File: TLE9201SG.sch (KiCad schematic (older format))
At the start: 6 parts, among them U4 TLE9201SG

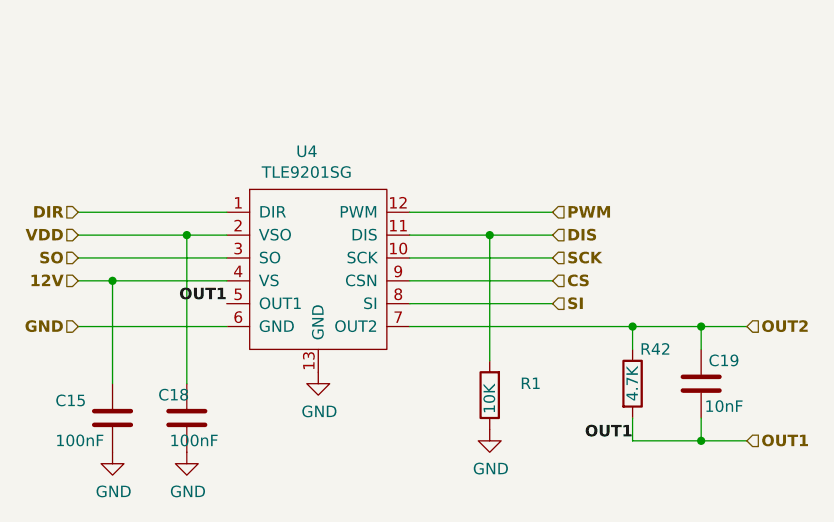
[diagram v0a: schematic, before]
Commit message: from Ola and Jared (#71)
* Update

* removed fp-info-cache from git

* Gerbers

* moved connector

* Mostly Ola's e-mailed copy, plus some of my own fixes to his almost done revision. I also did some house cleaning, with boundary edges, removed most DRC and ERC errors, etc.

* added Fiducial's
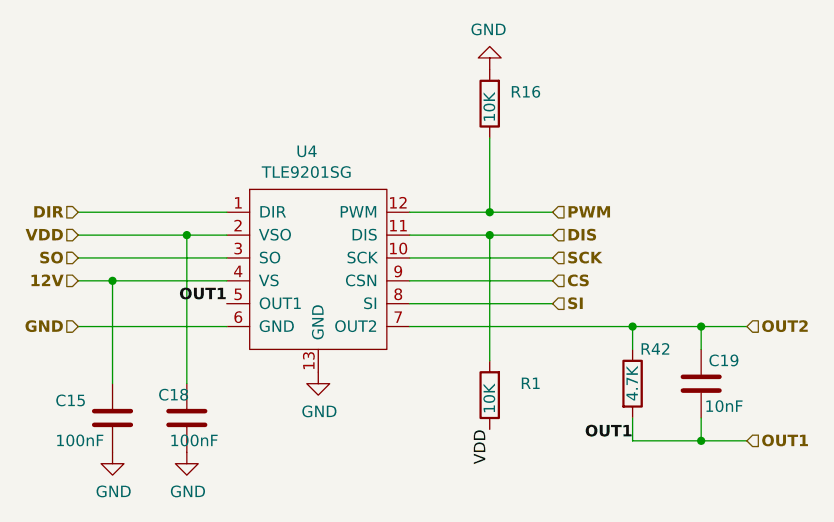
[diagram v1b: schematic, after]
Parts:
- added R16: 10K, Resistor_SMD:R_0603_1608Metric, symbol Device:R
- C15, C18, C19: footprint Capacitor_SMD:C_0603_1608Metric_Pad1.05x0.95mm_HandSolder -> Capacitor_SMD:C_0603_1608Metric
- R1, R42: footprint Resistor_SMD:R_0603_1608Metric_Pad1.05x0.95mm_HandSolder -> Resistor_SMD:R_0603_1608Metric
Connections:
- net GND: now also R16.2; no longer R1.1
- net PWM: now also R16.1
- net VDD: now also R1.1
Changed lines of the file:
@@
 EELAYER 29 0
 EELAYER END
-$Descr A4 11693 8268
+$Descr A 11000 8500
 encoding utf-8
 Sheet 4 7
 Title "microRusEfi"
-Date ""
-Rev ""
+Date "2019-07-01"
+Rev "R0.2"
 Comp ""
 Comment1 ""
@@
 GND
 Wire Wire Line
-	6750 3250 6125 3250
+	6750 3250 6475 3250
 Wire Wire Line
 	6750 3450 6125 3450
@@
 F 0 "C15" H 4575 4225 50  0000 L CNN
 F 1 "100nF" H 4575 4050 50  0000 L CNN
-F 2 "Capacitor_SMD:C_0603_1608Metric_Pad1.05x0.95mm_HandSolder" H 4863 4000 50  0001 C CNN
+F 2 "Capacitor_SMD:C_0603_1608Metric" H 4863 4000 50  0001 C CNN
 F 3 "~" H 4825 4150 50  0001 C CNN
 	1    4825 4150
@@
 F 0 "R1" H 6250 4000 50  0000 L CNN
 F 1 "10K" V 6475 4000 50  0000 L CNN
-F 2 "Resistor_SMD:R_0603_1608Metric_Pad1.05x0.95mm_HandSolder" V 6405 4050 50  0001 C CNN
+F 2 "Resistor_SMD:R_0603_1608Metric" V 6405 4050 50  0001 C CNN
 F 3 "~" H 6475 4050 50  0001 C CNN
 	1    6475 4050
@@
 L power:GND #PWR0161
 U 1 1 5E76AE52
-P 6475 4200
-F 0 "#PWR0161" H 6475 3950 50  0001 C CNN
-F 1 "GND" H 6480 4027 50  0000 C CNN
-F 2 "" H 6475 4200 50  0001 C CNN
-F 3 "" H 6475 4200 50  0001 C CNN
-	1    6475 4200
-	1    0    0    -1
+P 6475 2625
+F 0 "#PWR0161" H 6475 2375 50  0001 C CNN
+F 1 "GND" H 6480 2452 50  0000 C CNN
+F 2 "" H 6475 2625 50  0001 C CNN
+F 3 "" H 6475 2625 50  0001 C CNN
+	1    6475 2625
+	-1   0    0    1
 $EndComp
 Wire Wire Line
@@
 F 0 "C18" H 5025 4250 50  0000 L CNN
 F 1 "100nF" H 5075 4050 50  0000 L CNN
-F 2 "Capacitor_SMD:C_0603_1608Metric_Pad1.05x0.95mm_HandSolder" H 5188 4000 50  0001 C CNN
+F 2 "Capacitor_SMD:C_0603_1608Metric" H 5188 4000 50  0001 C CNN
 F 3 "~" H 5150 4150 50  0001 C CNN
 	1    5150 4150
@@
 F 0 "R42" H 7200 4150 50  0000 C CNN
 F 1 "4.7K" V 7100 4000 50  0000 C CNN
-F 2 "Resistor_SMD:R_0603_1608Metric_Pad1.05x0.95mm_HandSolder" H 7100 4000 50  0001 C CNN
+F 2 "Resistor_SMD:R_0603_1608Metric" H 7100 4000 50  0001 C CNN
 F 3 "~" H 7100 4000 50  0001 C CNN
 F 4 "MOUSER" H 1800 450 50  0001 C CNN "VEND"
@@
 F 0 "C19" H 7500 4100 50  0000 C CNN
 F 1 "10nF" H 7500 3900 50  0000 C CNN
-F 2 "Capacitor_SMD:C_0603_1608Metric_Pad1.05x0.95mm_HandSolder" H 7400 4000 50  0001 C CNN
+F 2 "Capacitor_SMD:C_0603_1608Metric" H 7400 4000 50  0001 C CNN
 F 3 "~" H 7400 4000 50  0001 C CNN
 	1    7400 4000
@@
 Wire Wire Line
 	4675 3350 5150 3350
+Text Label 6475 4200 3    50   ~ 0
+VDD
+Wire Wire Line
+	6475 3250 6475 2925
+Connection ~ 6475 3250
+Wire Wire Line
+	6475 3250 6125 3250
+$Comp
+L Device:R R16
+U 1 1 5D2D1AE3
+P 6475 2775
+F 0 "R16" H 6250 2725 50  0000 L CNN
+F 1 "10K" V 6475 2725 50  0000 L CNN
+F 2 "Resistor_SMD:R_0603_1608Metric" V 6405 2775 50  0001 C CNN
+F 3 "~" H 6475 2775 50  0001 C CNN
+	1    6475 2775
+	-1   0    0    1
+$EndComp
 $EndSCHEMATC

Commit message: Updated logo symbol and footprint, BOM is 99% entered in KC schematic now.
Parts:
- C15, C18: Manufacturer (none) -> KEMET; Part # (none) -> C0603C104J5RACTU; VEND (none) -> DIGI; VEND# (none) -> 399-7844-1-ND
- C19: Manufacturer (none) -> KEMET; Part # (none) -> C0603C103K1RACTU; VEND (none) -> DIGI; VEND# (none) -> 399-3189-1-ND
- R1, R16: Manufacturer (none) -> StackPole; Part # (none) -> RMCF0603JT10K0; VEND (none) -> DIGI; VEND# (none) -> RMCF0603JT10K0CT-ND
- R42: Manufacturer (none) -> StackPole; Part # (none) -> RMCF0603JT4K70; VEND MOUSER -> DIGI; VEND# (none) -> RMCF0603JT4K70CT-ND
- U4: Manufacturer (none) -> Infineon; Part # 726-TLE9201SG -> TLE9201SG; VEND (none) -> DIGI; VEND# (none) -> TLE9201SGAUMA1CT-ND
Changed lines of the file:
@@
 F 2 "Capacitor_SMD:C_0603_1608Metric" H 4863 4000 50  0001 C CNN
 F 3 "~" H 4825 4150 50  0001 C CNN
+F 4 "C0603C104J5RACTU" H 0   0   50  0001 C CNN "Part #"
+F 5 "DIGI" H 0   0   50  0001 C CNN "VEND"
+F 6 "399-7844-1-ND" H 0   0   50  0001 C CNN "VEND#"
+F 7 "KEMET" H 0   0   50  0001 C CNN "Manufacturer"
 	1    4825 4150
 	1    0    0    -1
@@
 F 2 "Resistor_SMD:R_0603_1608Metric" V 6405 4050 50  0001 C CNN
 F 3 "~" H 6475 4050 50  0001 C CNN
+F 4 "RMCF0603JT10K0" H 0   0   50  0001 C CNN "Part #"
+F 5 "DIGI" H 0   0   50  0001 C CNN "VEND"
+F 6 "RMCF0603JT10K0CT-ND" H 0   0   50  0001 C CNN "VEND#"
+F 7 "StackPole" H 0   0   50  0001 C CNN "Manufacturer"
 	1    6475 4050
 	-1   0    0    1
@@
 F 2 "Capacitor_SMD:C_0603_1608Metric" H 5188 4000 50  0001 C CNN
 F 3 "~" H 5150 4150 50  0001 C CNN
+F 4 "C0603C104J5RACTU" H 0   0   50  0001 C CNN "Part #"
+F 5 "DIGI" H 0   0   50  0001 C CNN "VEND"
+F 6 "399-7844-1-ND" H 0   0   50  0001 C CNN "VEND#"
+F 7 "KEMET" H 0   0   50  0001 C CNN "Manufacturer"
 	1    5150 4150
 	1    0    0    -1
@@
 F 2 "Resistor_SMD:R_0603_1608Metric" H 7100 4000 50  0001 C CNN
 F 3 "~" H 7100 4000 50  0001 C CNN
-F 4 "MOUSER" H 1800 450 50  0001 C CNN "VEND"
+F 4 "DIGI" H 1800 450 50  0001 C CNN "VEND"
+F 5 "RMCF0603JT4K70" H 0   0   50  0001 C CNN "Part #"
+F 6 "RMCF0603JT4K70CT-ND" H 0   0   50  0001 C CNN "VEND#"
+F 7 "StackPole" H 0   0   50  0001 C CNN "Manufacturer"
 	1    7100 4000
 	1    0    0    -1
@@
 F 2 "Capacitor_SMD:C_0603_1608Metric" H 7400 4000 50  0001 C CNN
 F 3 "~" H 7400 4000 50  0001 C CNN
+F 4 "C0603C103K1RACTU" H 0   0   50  0001 C CNN "Part #"
+F 5 "DIGI" H 0   0   50  0001 C CNN "VEND"
+F 6 "399-3189-1-ND" H 0   0   50  0001 C CNN "VEND#"
+F 7 "KEMET" H 0   0   50  0001 C CNN "Manufacturer"
 	1    7400 4000
 	1    0    0    -1
@@
 F 2 "Package_SO:Infineon_PG-DSO-12-11" H 5525 3100 50  0001 C CNN
 F 3 "" H 5525 3100 50  0001 C CNN
-F 4 "726-TLE9201SG" H 0   0   50  0001 C CNN "Part #"
+F 4 "TLE9201SG" H 0   0   50  0001 C CNN "Part #"
+F 5 "DIGI" H 0   0   50  0001 C CNN "VEND"
+F 6 "TLE9201SGAUMA1CT-ND" H 0   0   50  0001 C CNN "VEND#"
+F 7 "Infineon " H 0   0   50  0001 C CNN "Manufacturer"
 	1    5525 3100
 	1    0    0    -1
@@
 F 2 "Resistor_SMD:R_0603_1608Metric" V 6405 2775 50  0001 C CNN
 F 3 "~" H 6475 2775 50  0001 C CNN
+F 4 "RMCF0603JT10K0" H 0   0   50  0001 C CNN "Part #"
+F 5 "DIGI" H 0   0   50  0001 C CNN "VEND"
+F 6 "RMCF0603JT10K0CT-ND" H 0   0   50  0001 C CNN "VEND#"
+F 7 "StackPole" H 0   0   50  0001 C CNN "Manufacturer"
 	1    6475 2775
 	-1   0    0    1

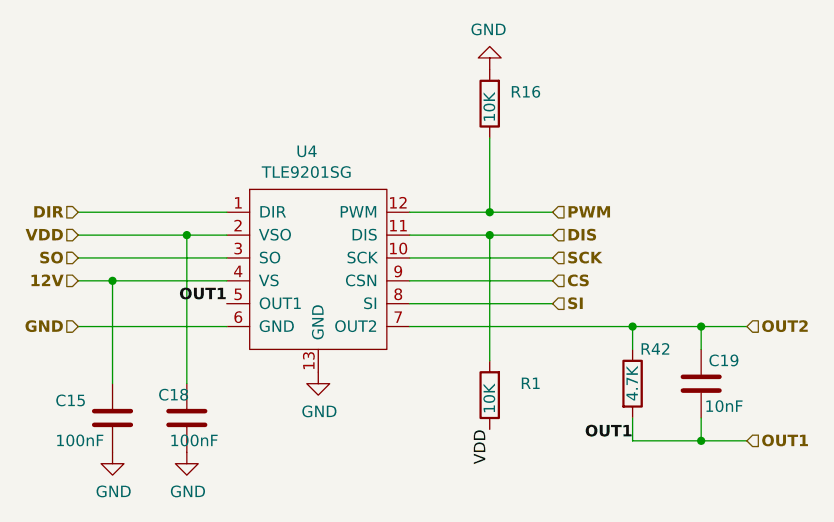
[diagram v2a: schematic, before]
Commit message: Updated 1k/1.5k resistor arrays, updated 2.7k's and R141. Changed several K's into k's for consistent ref designation names. https://github.com/rusefi/hw_microRusEfi/issues/51
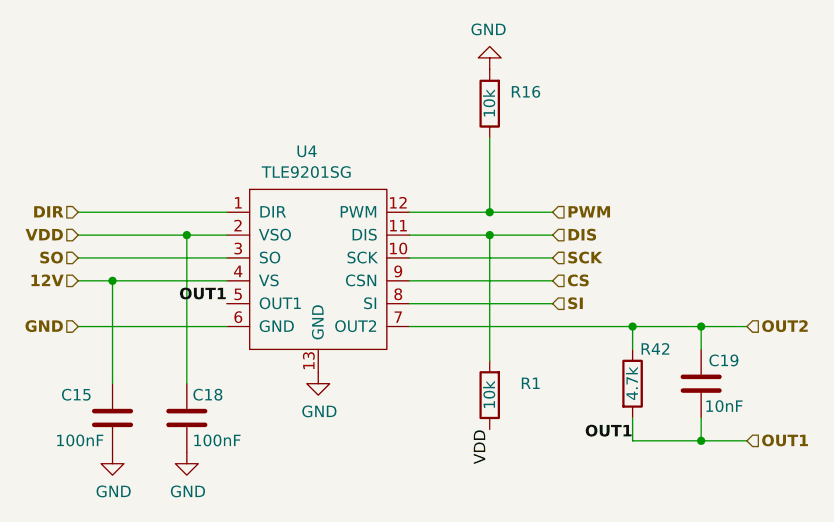
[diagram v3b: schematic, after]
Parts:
- R1, R16: value 10K -> 10k
- R42: value 4.7K -> 4.7k
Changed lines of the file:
@@
 U 1 1 5DE4B24C
 P 4825 4150
-F 0 "C15" H 4575 4225 50  0000 L CNN
+F 0 "C15" H 4600 4250 50  0000 L CNN
 F 1 "100nF" H 4575 4050 50  0000 L CNN
 F 2 "Capacitor_SMD:C_0603_1608Metric" H 4863 4000 50  0001 C CNN
@@
 P 6475 4050
 F 0 "R1" H 6250 4000 50  0000 L CNN
-F 1 "10K" V 6475 4000 50  0000 L CNN
+F 1 "10k" V 6475 4050 50  0000 C CNN
 F 2 "Resistor_SMD:R_0603_1608Metric" V 6405 4050 50  0001 C CNN
-F 3 "~" H 6475 4050 50  0001 C CNN
+F 3 "TBD" H 6475 4050 50  0001 C CNN
 F 4 "RMCF0603JT10K0" H 0   0   50  0001 C CNN "Part #"
 F 5 "DIGI" H 0   0   50  0001 C CNN "VEND"
@@
 U 1 1 5D324D41
 P 5150 4150
-F 0 "C18" H 5025 4250 50  0000 L CNN
-F 1 "100nF" H 5075 4050 50  0000 L CNN
+F 0 "C18" H 5175 4250 50  0000 L CNN
+F 1 "100nF" H 5175 4050 50  0000 L CNN
 F 2 "Capacitor_SMD:C_0603_1608Metric" H 5188 4000 50  0001 C CNN
 F 3 "~" H 5150 4150 50  0001 C CNN
@@
 P 7100 4000
 F 0 "R42" H 7200 4150 50  0000 C CNN
-F 1 "4.7K" V 7100 4000 50  0000 C CNN
+F 1 "4.7k" V 7100 4000 50  0000 C CNN
 F 2 "Resistor_SMD:R_0603_1608Metric" H 7100 4000 50  0001 C CNN
 F 3 "~" H 7100 4000 50  0001 C CNN
@@
 P 6475 2775
 F 0 "R16" H 6250 2725 50  0000 L CNN
-F 1 "10K" V 6475 2725 50  0000 L CNN
+F 1 "10k" V 6475 2775 50  0000 C CNN
 F 2 "Resistor_SMD:R_0603_1608Metric" V 6405 2775 50  0001 C CNN
-F 3 "~" H 6475 2775 50  0001 C CNN
+F 3 "TBD" H 6475 2775 50  0001 C CNN
 F 4 "RMCF0603JT10K0" H 0   0   50  0001 C CNN "Part #"
 F 5 "DIGI" H 0   0   50  0001 C CNN "VEND"

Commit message: sync (#98)
* Added silk screen mark, minor schematic formatting.
https://github.com/rusefi/hw_microRusEfi/issues/89

* Changed SWD connector to reflect validated brain board.
https://github.com/rusefi/hw_microRusEfi/issues/88

* Changed R26 into push button SW1 BOM is still TBD
https://github.com/rusefi/hw_microRusEfi/issues/86

* coil1 silk was corrected to coil2
https://github.com/rusefi/hw_microRusEfi/issues/90

* Updated BOM
https://github.com/rusefi/hw_microRusEfi/issues/94
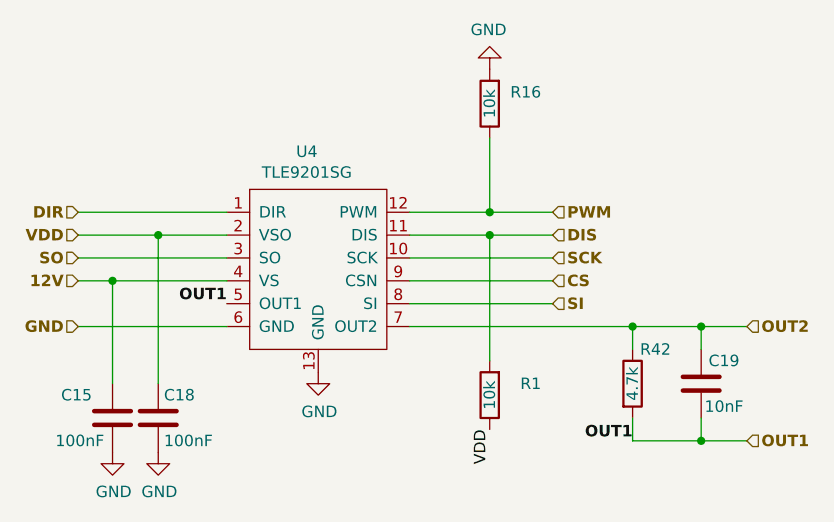
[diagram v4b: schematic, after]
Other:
- moved on the sheet: C18
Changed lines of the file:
@@
 L Device:C C18
 U 1 1 5D324D41
-P 5150 4150
-F 0 "C18" H 5175 4250 50  0000 L CNN
-F 1 "100nF" H 5175 4050 50  0000 L CNN
-F 2 "Capacitor_SMD:C_0603_1608Metric" H 5188 4000 50  0001 C CNN
-F 3 "~" H 5150 4150 50  0001 C CNN
-F 4 "C0603C104J5RACTU" H 0   0   50  0001 C CNN "Part #"
-F 5 "DIGI" H 0   0   50  0001 C CNN "VEND"
-F 6 "399-7844-1-ND" H 0   0   50  0001 C CNN "VEND#"
-F 7 "KEMET" H 0   0   50  0001 C CNN "Manufacturer"
-	1    5150 4150
+P 5025 4150
+F 0 "C18" H 5050 4250 50  0000 L CNN
+F 1 "100nF" H 5050 4050 50  0000 L CNN
+F 2 "Capacitor_SMD:C_0603_1608Metric" H 5063 4000 50  0001 C CNN
+F 3 "~" H 5025 4150 50  0001 C CNN
+F 4 "C0603C104J5RACTU" H -125 0   50  0001 C CNN "Part #"
+F 5 "DIGI" H -125 0   50  0001 C CNN "VEND"
+F 6 "399-7844-1-ND" H -125 0   50  0001 C CNN "VEND#"
+F 7 "KEMET" H -125 0   50  0001 C CNN "Manufacturer"
+	1    5025 4150
 	1    0    0    -1
 $EndComp
@@
 L power:GND #PWR0189
 U 1 1 5D324D4B
-P 5150 4300
-F 0 "#PWR0189" H 5150 4050 50  0001 C CNN
-F 1 "GND" H 5155 4127 50  0000 C CNN
-F 2 "" H 5150 4300 50  0001 C CNN
-F 3 "" H 5150 4300 50  0001 C CNN
-	1    5150 4300
+P 5025 4300
+F 0 "#PWR0189" H 5025 4050 50  0001 C CNN
+F 1 "GND" H 5030 4127 50  0000 C CNN
+F 2 "" H 5025 4300 50  0001 C CNN
+F 3 "" H 5025 4300 50  0001 C CNN
+	1    5025 4300
 	1    0    0    -1
 $EndComp
 Wire Wire Line
-	5150 4000 5150 3350
+	5025 4000 5025 3350
 $Comp
 L Device:R R42
@@
 Text Label 7100 4250 2    50   ~ 10
 OUT1
-Connection ~ 5150 3350
+Connection ~ 5025 3350
 Wire Wire Line
-	5150 3350 5325 3350
+	5025 3350 5325 3350
 Wire Wire Line
-	4675 3350 5150 3350
+	4675 3350 5025 3350
 Text Label 6475 4200 3    50   ~ 0
 VDD

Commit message: R0.3 released
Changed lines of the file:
@@
 Wire Wire Line
 	4675 3350 5025 3350
-Text Label 6475 4200 3    50   ~ 0
+Text Label 6475 4200 3    50   ~ 6
 VDD
 Wire Wire Line

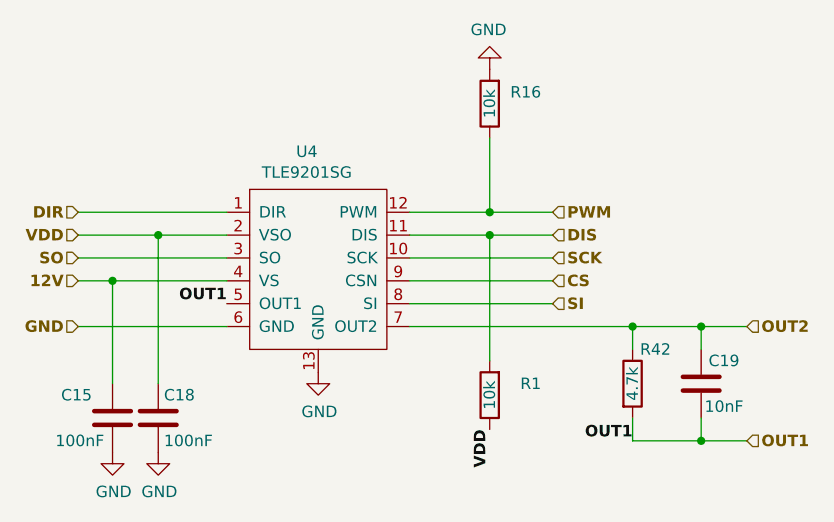
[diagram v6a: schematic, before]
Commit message: Significant revision of schematic and layout:
Added reverse voltage protection.
Split 12V supply into a 12V-Key (ignition) pin and a 12V-MRel (supply from
main relay) pin.  The 12V main relay is controlled by the MRel pin to protect against reverse voltage and over-voltage.

The board can optionally draw under 1mA from the main relay coil to power
standby features, including CAN monitoring.

Increased the size of several resistors, notably ignition output resistors
and CAN termination, to handle typical power draw.

Changed resistor dividers to individual resistors for better accuracy than
typical resistor networks.

Standardized pull-up and pull-down resistors to 10K.

Changed to a tab-output regulator.
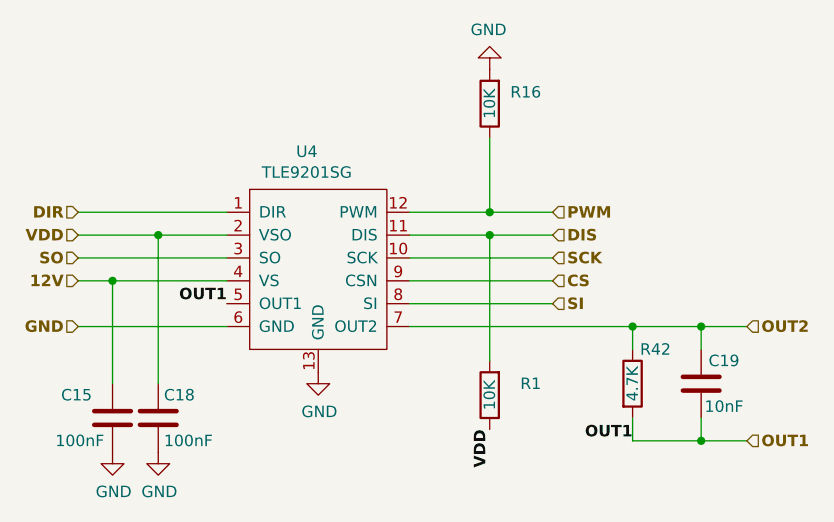
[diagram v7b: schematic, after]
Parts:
- C15, C18: LCSC (none) -> C14663
- C19: LCSC (none) -> C57112
- R1, R16: value 10k -> 10K; LCSC (none) -> C25804
- R42: value 4.7k -> 4.7K; LCSC (none) -> C23162
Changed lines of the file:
@@
 F 6 "399-7844-1-ND" H 0   0   50  0001 C CNN "VEND#"
 F 7 "KEMET" H 0   0   50  0001 C CNN "Manufacturer"
+F 8 "C14663" H 4825 4150 50  0001 C CNN "LCSC"
 	1    4825 4150
 	1    0    0    -1
@@
 P 6475 4050
 F 0 "R1" H 6250 4000 50  0000 L CNN
-F 1 "10k" V 6475 4050 50  0000 C CNN
+F 1 "10K" V 6475 4050 50  0000 C CNN
 F 2 "Resistor_SMD:R_0603_1608Metric" V 6405 4050 50  0001 C CNN
 F 3 "TBD" H 6475 4050 50  0001 C CNN
@@
 F 6 "RMCF0603JT10K0CT-ND" H 0   0   50  0001 C CNN "VEND#"
 F 7 "StackPole" H 0   0   50  0001 C CNN "Manufacturer"
+F 8 "C25804" H 6475 4050 50  0001 C CNN "LCSC"
 	1    6475 4050
 	-1   0    0    1
@@
 F 6 "399-7844-1-ND" H -125 0   50  0001 C CNN "VEND#"
 F 7 "KEMET" H -125 0   50  0001 C CNN "Manufacturer"
+F 8 "C14663" H 5025 4150 50  0001 C CNN "LCSC"
 	1    5025 4150
 	1    0    0    -1
@@
 P 7100 4000
 F 0 "R42" H 7200 4150 50  0000 C CNN
-F 1 "4.7k" V 7100 4000 50  0000 C CNN
+F 1 "4.7K" V 7100 4000 50  0000 C CNN
 F 2 "Resistor_SMD:R_0603_1608Metric" H 7100 4000 50  0001 C CNN
 F 3 "~" H 7100 4000 50  0001 C CNN
@@
 F 6 "RMCF0603JT4K70CT-ND" H 0   0   50  0001 C CNN "VEND#"
 F 7 "StackPole" H 0   0   50  0001 C CNN "Manufacturer"
+F 8 "C23162" H 7100 4000 50  0001 C CNN "LCSC"
 	1    7100 4000
 	1    0    0    -1
@@
 F 6 "399-3189-1-ND" H 0   0   50  0001 C CNN "VEND#"
 F 7 "KEMET" H 0   0   50  0001 C CNN "Manufacturer"
+F 8 "C57112" H 7400 4000 50  0001 C CNN "LCSC"
 	1    7400 4000
 	1    0    0    -1
@@
 P 6475 2775
 F 0 "R16" H 6250 2725 50  0000 L CNN
-F 1 "10k" V 6475 2775 50  0000 C CNN
+F 1 "10K" V 6475 2775 50  0000 C CNN
 F 2 "Resistor_SMD:R_0603_1608Metric" V 6405 2775 50  0001 C CNN
 F 3 "TBD" H 6475 2775 50  0001 C CNN
@@
 F 6 "RMCF0603JT10K0CT-ND" H 0   0   50  0001 C CNN "VEND#"
 F 7 "StackPole" H 0   0   50  0001 C CNN "Manufacturer"
+F 8 "C25804" H 6475 2775 50  0001 C CNN "LCSC"
 	1    6475 2775
 	-1   0    0    1
